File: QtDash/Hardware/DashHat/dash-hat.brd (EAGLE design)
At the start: 120.9 x 66.8 mm, 169 parts, among them IC1 LMV614, IC2 MCP3X083008, IC3 MCP23017SS, IC4 LM358D, IC5 IL300, IC6 TSV912D, IC7 IL300, IC8 TSV912D, IC9 DS1374, J1 CONN_20X2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

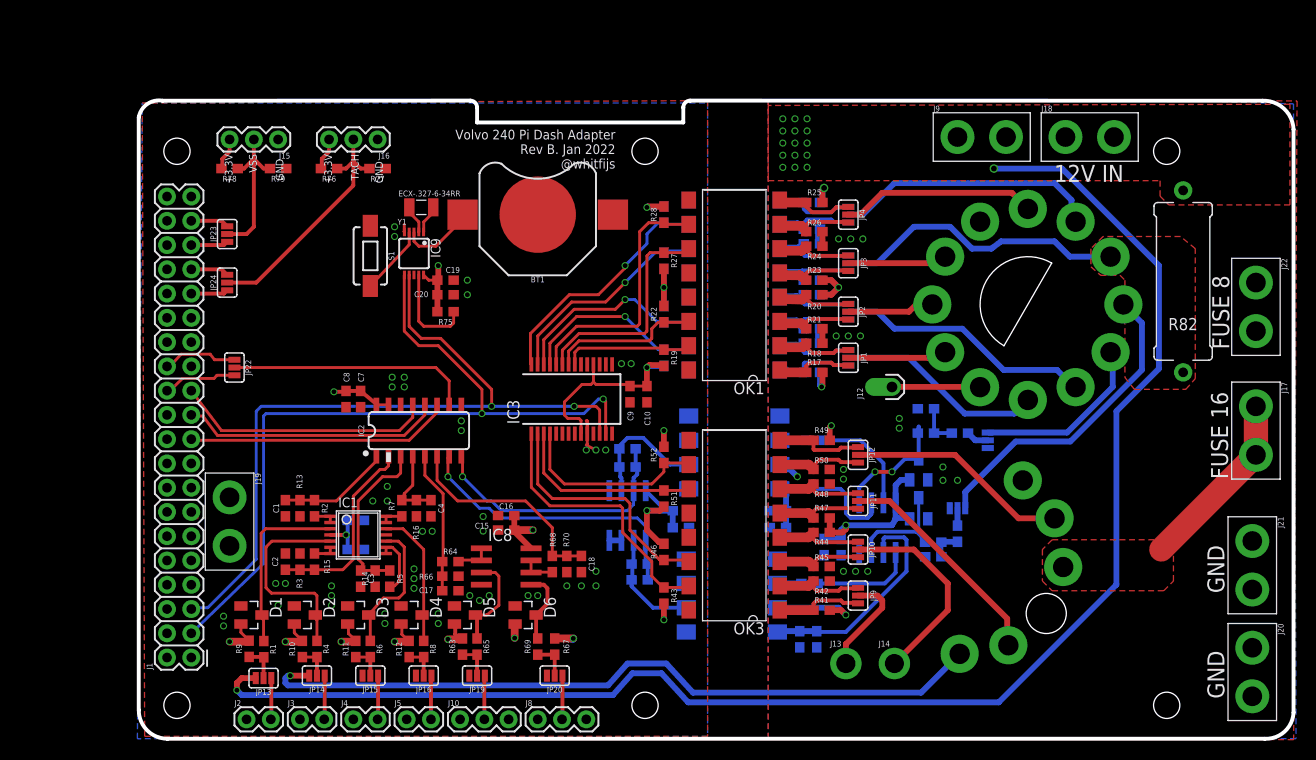
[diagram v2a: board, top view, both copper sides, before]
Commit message: topix/component-optimization: 	- fixed issue with gauge needle movement 	- changed sensor 5V to 3.3V resistor divider to use resistory arrays
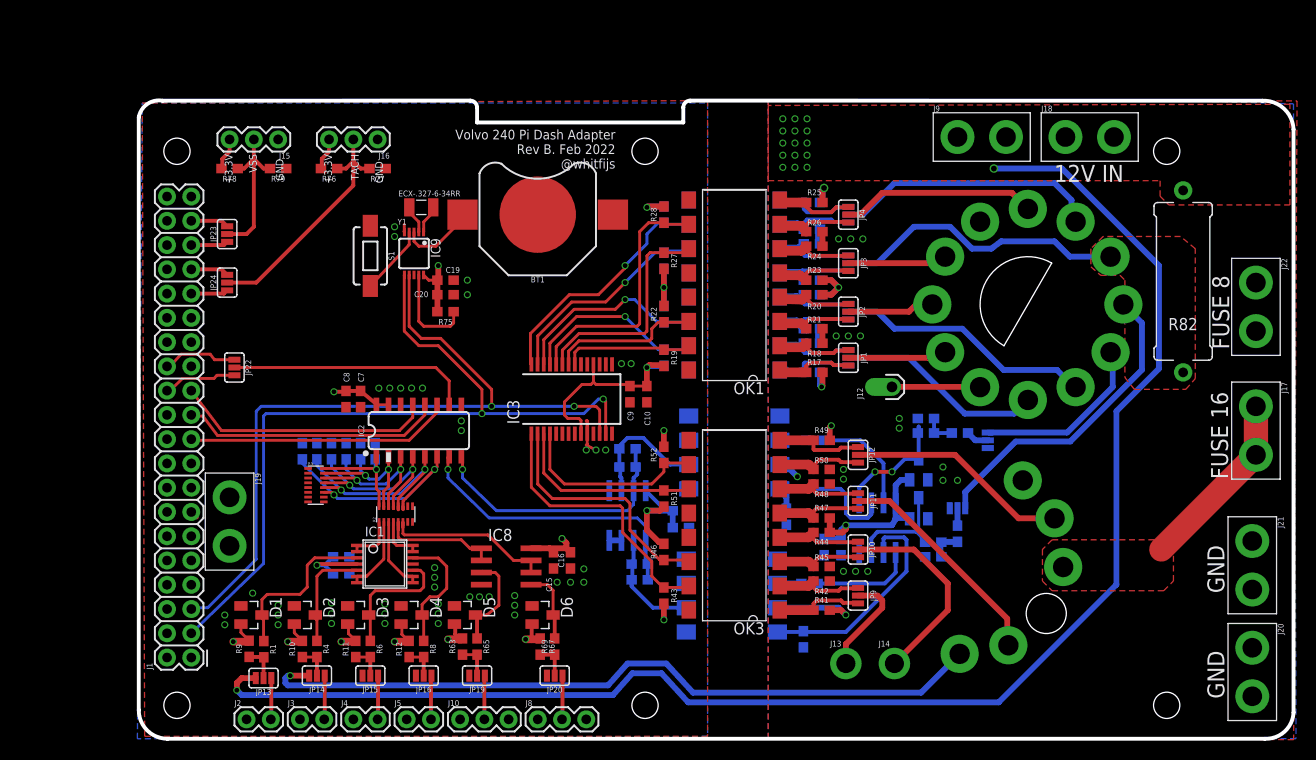
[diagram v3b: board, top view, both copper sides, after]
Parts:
- removed R13, R14, R15, R16, R66, R70: 620k, digital_dash:0603
- removed R5, R64, R68, R7: 330k, digital_dash:0603
- removed R54, R60: 1M, digital_dash:0603
- C1, C17, C18, C2, C3, C4: value 10n -> 100n
- R2: value 330k -> 8.2k; device digital_dash:0603 -> digital_dash:YC248
- R3: value 330k -> 15k; device digital_dash:0603 -> digital_dash:YC248
- R53, R59: value 1M -> 499k 1%
- R71, R72, R73, R74: value 100k -> 100k 1%
- moved C18 31.5 mm to (17.3, 30.1), flipped to the bottom, turned to 90 degrees
- moved C17 20.2 mm to (18.8, 30.1), flipped to the bottom, turned to 90 degrees
- moved C2 14.0 mm to (23.4, 30.1), flipped to the bottom
- moved C3 13.4 mm to (21.8, 30.1), flipped to the bottom, turned to 90 degrees
- moved C4 12.0 mm to (20.3, 30.1), flipped to the bottom, turned to 90 degrees
- moved C1 11.1 mm to (24.9, 30.1), flipped to the bottom, turned to 90 degrees
- moved R2 8.53 mm to (27.1, 23.5), turned to 90 degrees
- moved C16 8.21 mm to (45.3, 18.7), turned to 270 degrees
- moved R3 8.00 mm to (18.7, 26.5), turned to 0 degrees
- moved C15 5.88 mm to (43.6, 18.7), turned to 270 degrees
- moved IC1 4.13 mm to (25.9, 18.3)
- moved C5 4.10 mm to (21.3, 19.1)
- moved C6 2.96 mm to (21.3, 17.3)
- moved R69 1.78 mm to (43.7, 9.65)
- moved D6 1.78 mm to (42.4, 13.0)
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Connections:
- net ADC1_IN: now also R2.16, R3.16; no longer R13.2, R2.1
- net ADC2_IN: now also R2.15, R3.15; no longer R15.2, R3.1
- net ADC3_IN: now also R2.14, R3.14; no longer R14.2, R5.1
- net ADC4_IN: now also R2.13, R3.13; no longer R16.2, R7.1
- net ADC5_IN: now also R2.12, R3.12; no longer R64.1, R66.2
- net ADC6_IN: now also R2.11, R3.11; no longer R68.1, R70.2
- net GND: now also R3.1, R3.2, R3.3, R3.4, R3.5, R3.6; no longer R13.1, R14.1, R15.1, R16.1, R66.1, R70.1
- net GND-ISO: no longer R54.1, R60.1
- net N$1: now also R2.1; no longer R2.2
- net N$13: now also R2.4; no longer R7.2
- net N$28: now also R2.5; no longer R64.2
- net N$35: now also R2.6; no longer R68.2
- net N$4: no longer R54.2
- net N$5: now also R2.2; no longer R3.2
- net N$8: no longer R60.2
- net N$9: now also R2.3; no longer R5.2
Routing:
- net N$35: track 3.51 -> 17.7 mm
- net ADC4_IN: track 8.04 -> 20.5 mm, vias 0 -> 2
- net N$7: track 21.8 -> 11.4 mm
- net N$28: track 3.73 -> 13.0 mm
- net ADC5_IN: track 14.9 -> 23.3 mm, vias 0 -> 2
- net N$5: track 2.31 -> 8.10 mm
- net ADC2_IN: track 20.2 -> 15.2 mm, vias 0 -> 2
- net N$1: track 2.31 -> 5.32 mm
- net ADC6_IN: track 22.6 -> 25.6 mm, vias 0 -> 2
- net N$8: track 17.7 -> 15.5 mm
- net N$13: track 2.80 -> 4.94 mm
- net 5V: track 33.6 -> 35.3 mm, vias 9 -> 8
- net N$3: track 18.8 -> 17.5 mm
- net N$9: track 6.73 -> 7.90 mm
- net N$15: track 14.5 -> 13.4 mm
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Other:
- board text added: "Volvo 240 Pi Dash Adapter Rev B. Feb 2022 @whitfijs"
- board text removed: "Volvo 240 Pi Dash Adapter Rev B. Jan 2022 @whitfijs"

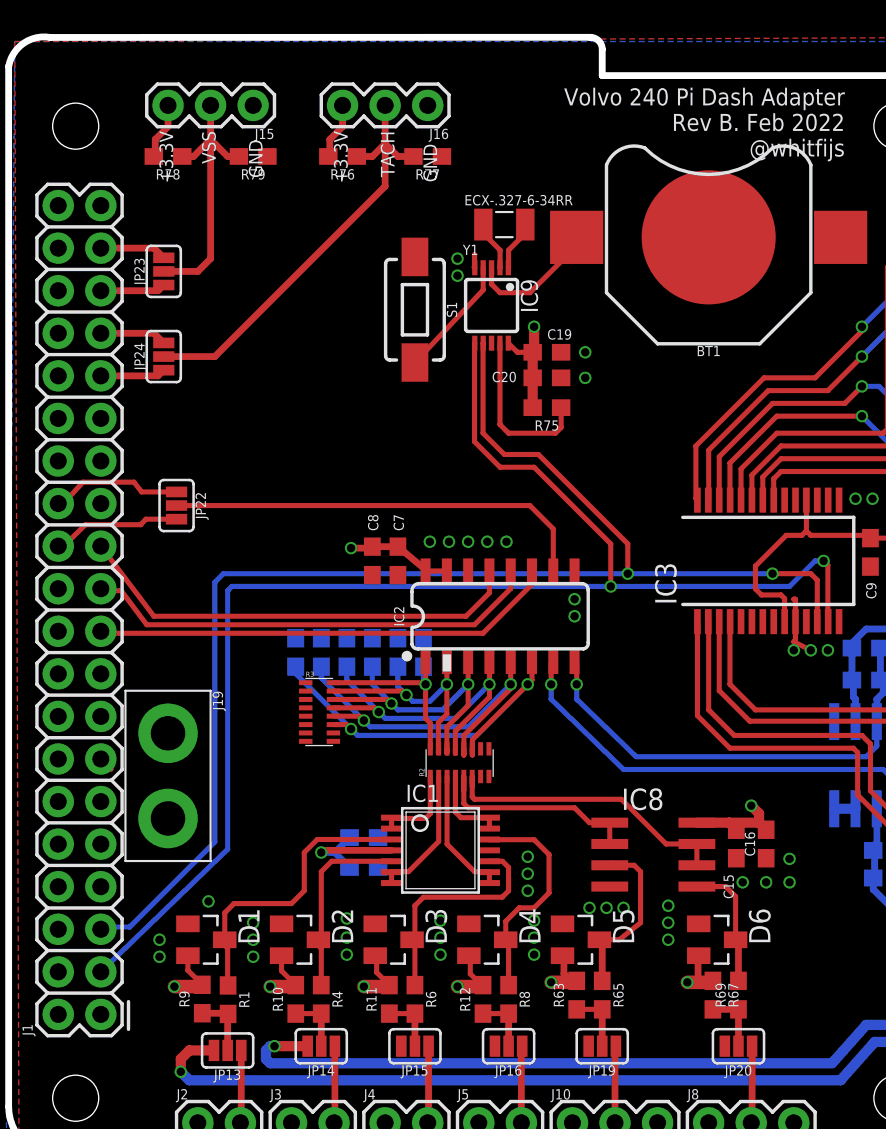
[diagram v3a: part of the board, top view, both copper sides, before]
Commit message: topic/component-optimization: 	- re-organized schematic 	- fixed some layout issues and component labels on the board
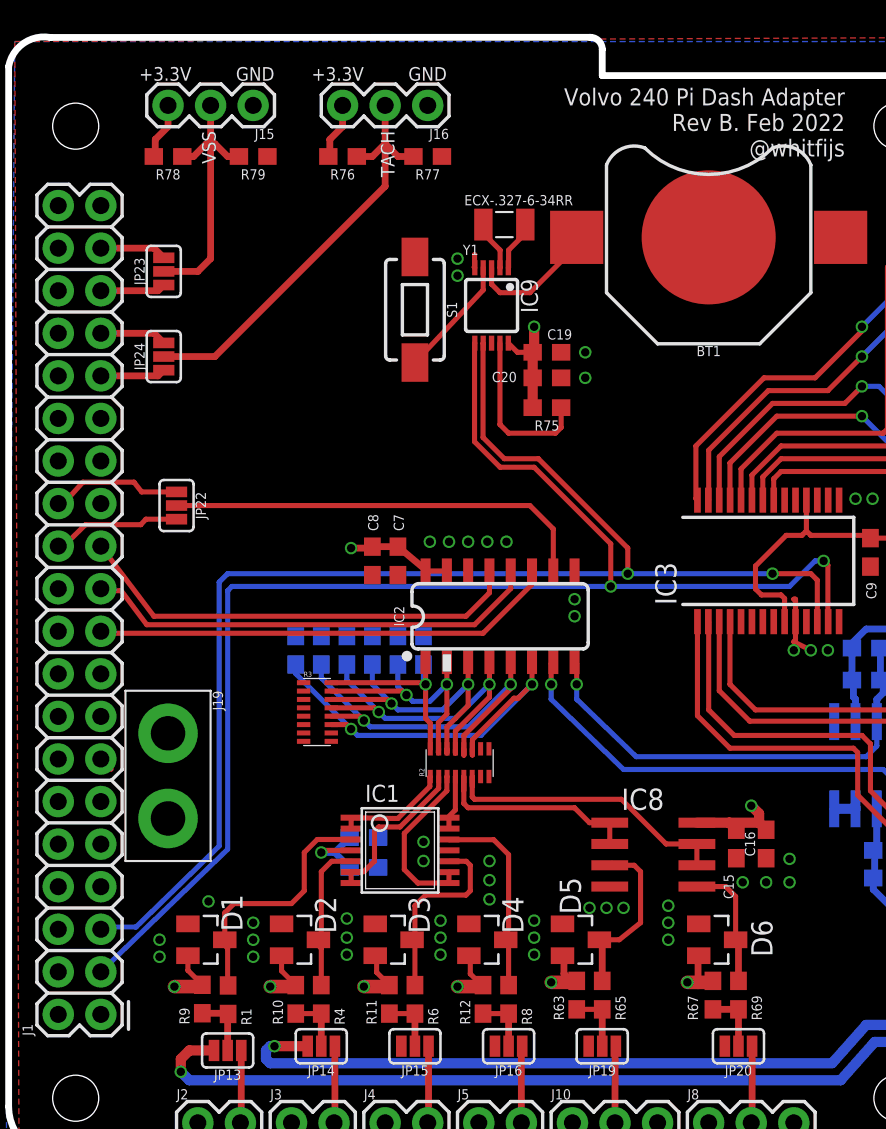
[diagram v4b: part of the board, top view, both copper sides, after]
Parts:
- moved IC1 2.41 mm to (23.5, 18.3)
- moved C1 0.13 mm to (24.9, 30.2)
- moved C17 0.13 mm to (18.8, 30.2)
- moved C18 0.13 mm to (17.3, 30.2)
- moved C2 0.13 mm to (23.4, 30.2)
- moved C3 0.13 mm to (21.8, 30.2)
- moved C4 0.13 mm to (20.3, 30.2)
- moved R3 0.13 mm to (18.5, 26.5)
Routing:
- net 5V: track 35.3 -> 32.9 mm
- net N$7: track 11.4 -> 8.95 mm
- net N$3: track 17.5 -> 15.1 mm
- net N$9: track 7.90 -> 10.3 mm
- net N$11: track 13.6 -> 11.5 mm
- net N$5: track 8.10 -> 9.69 mm
- net N$13: track 4.94 -> 3.38 mm
- net N$15: track 13.4 -> 11.9 mm
- net N$1: track 5.32 -> 6.74 mm
- net ADC6_IN: track 25.6 -> 26.3 mm
- net GND: vias 44 -> 46

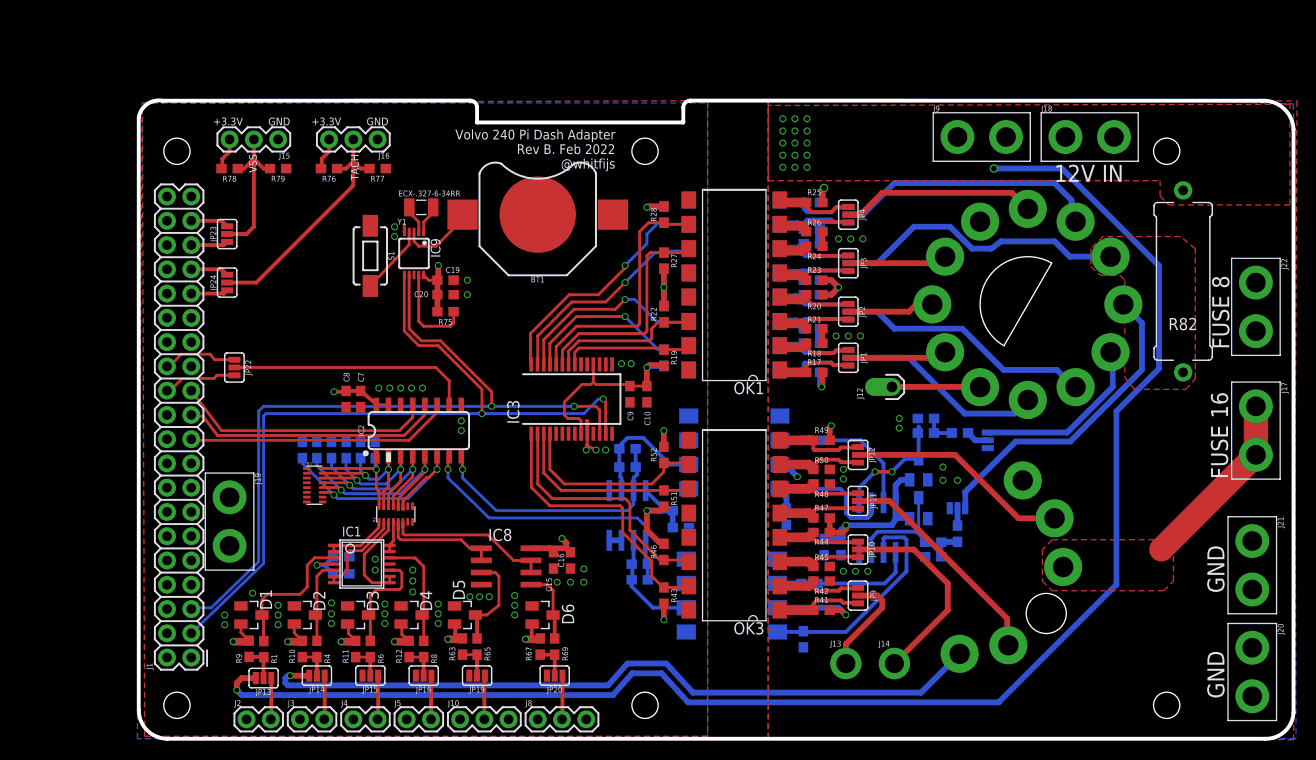
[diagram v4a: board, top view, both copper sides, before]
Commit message: topic-component-optimization: 	- added VSS circuit to isolated side of the board 	- removed superfluous jumpers for VSS input 	- re-arranged component labels 	- board sent off to JLCPCB
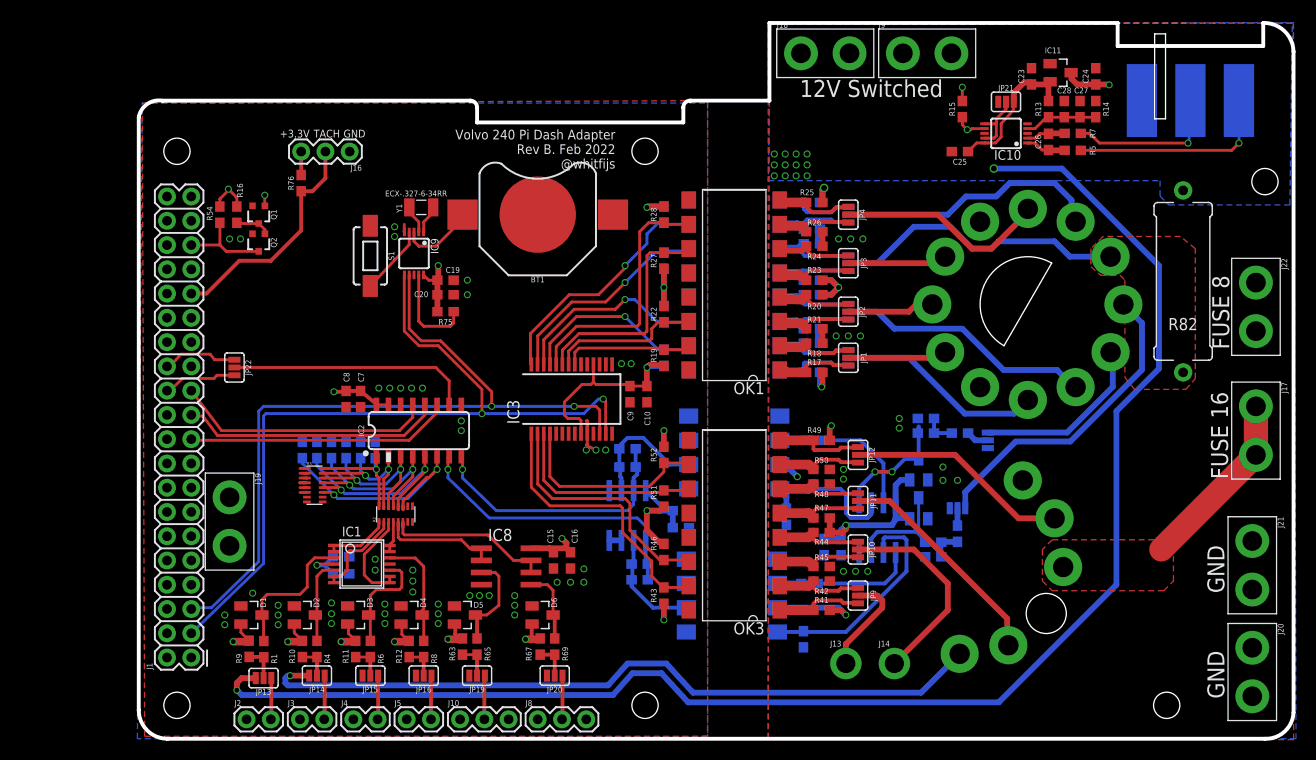
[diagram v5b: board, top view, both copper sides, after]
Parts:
- removed J12: (no value), SparkFun-Connectors:1X01_OFFSET
- removed J15: VSS_IN, SparkFun-Connectors:1X03
- removed JP23, JP24: TACH_INPUT_SEL, SparkFun-Jumpers:SMT-JUMPER_3_NO_SILK
- removed R77, R78, R79: 1k, digital_dash:0603
- added C23, C25, C27: 100n, digital_dash:0603
- added C24: 1u, digital_dash:0603
- added C26: 1n, digital_dash:0603
- added C28: 10u, digital_dash:0603
- added IC10: MAX9924, digital_dash:UMAX10
- added IC11: ZXTR2105FQ, digital_dash:SOT23
- added J11: VOLVO_CONN_VSS, digital_dash:VOLVO_CONN_VSS
- added JP21: SPI_CS_SEL, SparkFun-Jumpers:SMT-JUMPER_3_NO_SILK
- added Q1, Q2: 310mA/60V/1.6Ω, SparkFun-DiscreteSemi:SOT323
- added R13, R14, R15, R16, R54: 1k, digital_dash:0603
- added R5, R7: 10k 1%, digital_dash:0603
- moved J18 29.0 mm to (72.0, 71.8)
- moved J9 10.5 mm to (82.7, 71.8)
- moved R76 3.29 mm to (17.1, 58.2), turned to 90 degrees
- moved J16 3.19 mm to (22.2, 61.5)
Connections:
- removed net N$33: J15.2, JP23.2, R78.1, R79.2
- removed net N$43: J16.2, JP24.2, R76.1, R77.2
- new net N$14: Q1.3, Q2.1, R16.1
- new net N$46: C26.1, IC10.1, R5.2
- new net N$47: C26.2, IC10.2, R7.2
- new net N$48: J11.G, R5.1
- new net N$49: J11.1, R7.1
- new net N$50: C27.1, C28.2, IC10.4, R13.1, R14.1
- new net N$52: IC10.6, IC10.9, JP21.2
- new net VCCA: C23.1, C25.1, IC10.10, IC11.2, JP21.3, R13.2
- net 12V: now also C24.1, IC11.3, J11.+, R15.2
- net 3.3V: now also R16.2, R54.2; no longer J15.3, R78.2
- net AC_RELAY/VSS_TO_ECU: now also IC10.7, Q1.1, R15.1; no longer J12.1
- net GND: now also Q1.2, Q2.2; no longer J15.1, R77.1, R79.1
- net GND-ISO: now also C23.2, C24.2, C25.2, C27.2, C28.1, IC10.5, IC11.1, JP21.1, R14.2
- net GPIO13: no longer JP24.3
- net GPIO19: now also Q2.3, R54.1; no longer JP23.1
- net GPIO26: no longer JP23.3
- net GPIO6: now also J16.2, R76.1; no longer JP24.1
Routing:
- net AC_RELAY/VSS_TO_ECU: track 9.22 -> 111.5 mm, vias 0 -> 2
- net N$43: track 26.3 -> 0.00 mm
- net N$48: track 0.00 -> 21.3 mm, vias 0 -> 1
- net GPIO6: track 3.90 -> 24.2 mm
- net N$33: track 16.3 -> 0.00 mm
- net N$49: track 0.00 -> 16.3 mm, vias 0 -> 1
- net VCCA: track 0.00 -> 16.1 mm
- net N$50: track 0.00 -> 7.64 mm
- net 12V: track 48.0 -> 54.9 mm, vias 22 -> 21
- net N$52: track 0.00 -> 6.61 mm
- net GPIO19: track 3.90 -> 9.66 mm
- net GND: track 7.30 -> 12.2 mm, vias 46 -> 48
- net N$46: track 0.00 -> 4.21 mm
- net N$47: track 0.00 -> 4.09 mm
- net GPIO26: track 3.99 -> 0.00 mm
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- added copper zone on layer 16, net 12V
- removed copper zone on layer 1, net 12V
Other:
- board size 120.9 x 66.8 mm -> 120.9 x 74.9 mm
- board text added: "12V Switched"
- board text removed: "12V IN"
- board text removed: "VSS"
